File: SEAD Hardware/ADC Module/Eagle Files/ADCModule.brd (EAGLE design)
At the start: 44.9 x 48.9 mm, 49 parts, among them IC2 93-C46AST, U1 LP2989_DGK_8, X1 52885-0374

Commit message: More layout work.
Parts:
- moved C19 18.3 mm to (2.50, 9.70), turned to 0 degrees
- moved U1 18.0 mm to (2.60, 5.70)
- moved C18 16.8 mm to (4.80, 2.90), turned to 270 degrees
- moved C7 16.7 mm to (2.50, 1.80)
- moved L2 13.1 mm to (8.90, 9.50)
- moved C24 13.1 mm to (8.90, 11.1)
- moved C12 13.0 mm to (32.9, 7.20)
- moved C11 13.0 mm to (26.3, 7.12)
- moved C15 13.0 mm to (40.4, 16.1)
- moved C16 13.0 mm to (40.4, 13.3)
- moved C14 13.0 mm to (40.4, 19.8)
- moved R6 13.0 mm to (2.50, 22.7)
- moved R7 13.0 mm to (2.50, 24.2)
- moved C23 13.0 mm to (14.3, 11.1)
- moved LED1 13.0 mm to (39.3, 9.87)
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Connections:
- removed net N$24: C18.2, C7.1, U1.3
- net GND: now also C18.2, C7.1, U1.3
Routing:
- net CANRX: track 0.00 -> 51.4 mm, vias 0 -> 3
- net CANTX: track 0.00 -> 46.3 mm, vias 0 -> 1
- net A0: track 0.00 -> 26.4 mm, vias 0 -> 2
- net WR*: track 0.00 -> 18.3 mm, vias 0 -> 2
- net RD*: track 0.00 -> 17.0 mm, vias 0 -> 2
- net VDD5V0_D: track 0.00 -> 16.9 mm
- net D4: track 5.34 -> 20.7 mm, vias 0 -> 2
- net D3: track 3.70 -> 18.8 mm, vias 0 -> 2
- net CS*: track 0.00 -> 13.2 mm
- net N$11: track 25.1 -> 12.0 mm
- net N$10: track 25.0 -> 11.9 mm
- net USB_UART_RX: track 19.3 -> 31.4 mm
- net USB_UART_TX: track 18.7 -> 30.5 mm
- net D2: track 0.00 -> 11.6 mm, vias 0 -> 2
- net D7: track 11.5 -> 22.9 mm
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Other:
- board size 44.9 x 48.9 mm -> 44.9 x 35.9 mm

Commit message: Finished DAQ revision.
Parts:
- added C25, C26, C27, C28: .1uF, SensorCape:0805
- moved C20 8.81 mm to (15.1, 30.9), turned to 180 degrees
- moved C13 8.61 mm to (38.3, 33.6), turned to 270 degrees
- moved C9 7.20 mm to (36.7, 33.6), turned to 270 degrees
- moved C15 6.48 mm to (41.4, 22.5)
- moved LED1 6.32 mm to (41.3, 15.9)
- moved R3 6.32 mm to (43.0, 15.9)
- moved C16 6.08 mm to (41.4, 19.3)
- moved U$1 6.08 mm to (31.9, 22.5)
- moved C1 6.00 mm to (35.0, 33.6)
- moved C2 6.00 mm to (27.0, 33.6)
- moved U$2 6.00 mm to (31.0, 33.6)
- moved C14 5.59 mm to (41.4, 25.3)
- moved C11 5.10 mm to (27.3, 12.1)
- moved C17 5.10 mm to (30.5, 12.1)
- moved C12 5.10 mm to (33.9, 12.2)
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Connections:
- net VDD1V8_D renamed VCC1V8_D
- net CANRX: no longer X1.7
- net CANTX: no longer X1.9
- net GND: now also C25.1, C26.1, C27.1, C28.1
- net VDD3V3_D: now also C25.2, C26.2, C27.2, C28.2
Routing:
- net VDD5V0_D: track 16.9 -> 97.0 mm, vias 0 -> 2
- net CANRX: track 51.4 -> 0.00 mm, vias 3 -> 0
- net CANTX: track 46.3 -> 0.00 mm, vias 1 -> 0
- net VDD3V3_D: track 19.0 -> 64.3 mm, vias 0 -> 21
- net GND: track 33.4 -> 21.8 mm, vias 12 -> 11
- net WR*: track 18.3 -> 7.55 mm, vias 2 -> 0
- net MCLR: track 3.24 -> 13.6 mm
- net RD*: track 17.0 -> 7.59 mm, vias 2 -> 0
- net D0: track 9.63 -> 17.6 mm, vias 0 -> 2
- net D3: track 18.8 -> 25.3 mm
- net PGC: track 7.54 -> 13.6 mm
- net MISO: track 21.0 -> 16.2 mm
- net PGD: track 10.9 -> 15.6 mm
- net CS*: track 13.2 -> 17.5 mm, vias 0 -> 2
- net USB_UART_TX: track 30.5 -> 26.4 mm
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- added copper zone on layer 15, net GND
- added copper zone on layer 14, net VDD3V3_D
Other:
- board size 44.9 x 35.9 mm -> 44.9 x 36.3 mm
- board text added: "SEAD DAQ Unit v1.3 (c) Pavlo Manovi - 2014 pavlo.me"
- board text removed: "SEAD DAQ Unit v1.2 (c) Pavlo Manovi - 2014 pavlo.me"

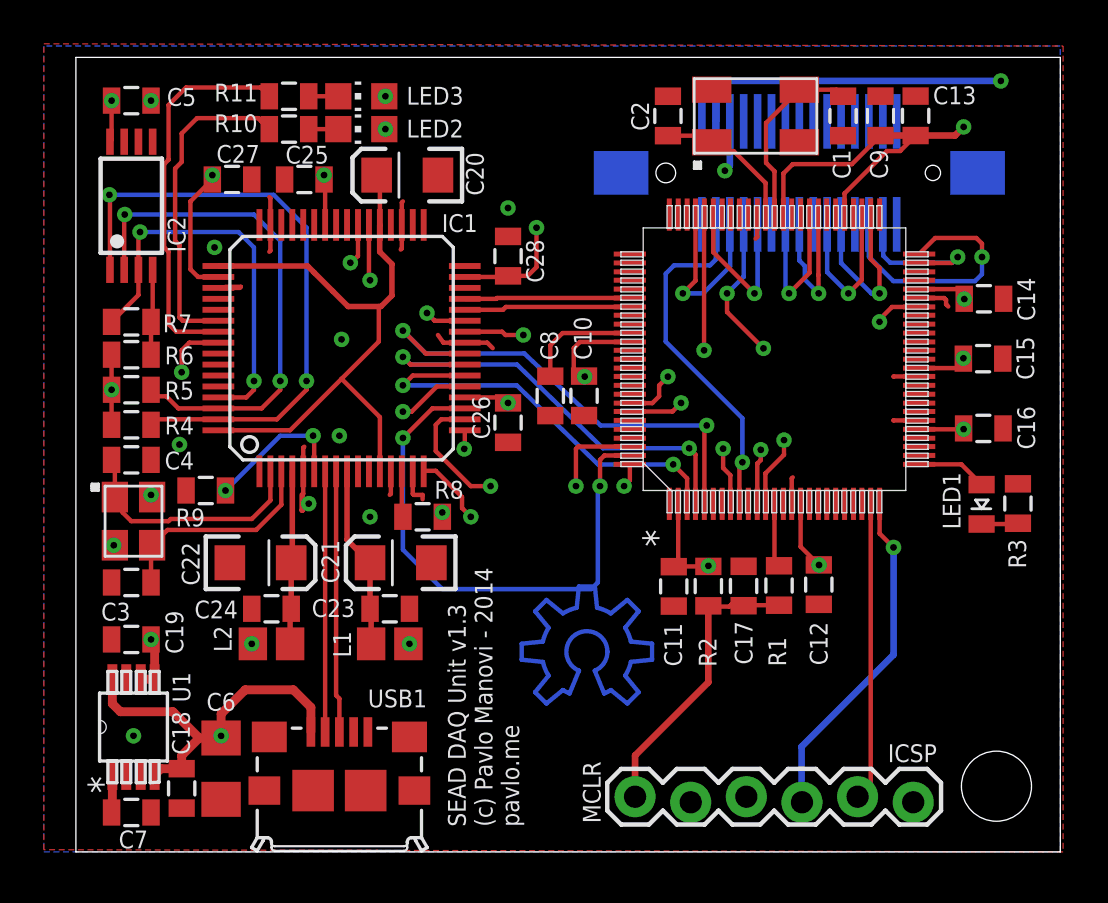
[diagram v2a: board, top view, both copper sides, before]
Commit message: Started ADC Hat. Library additions.
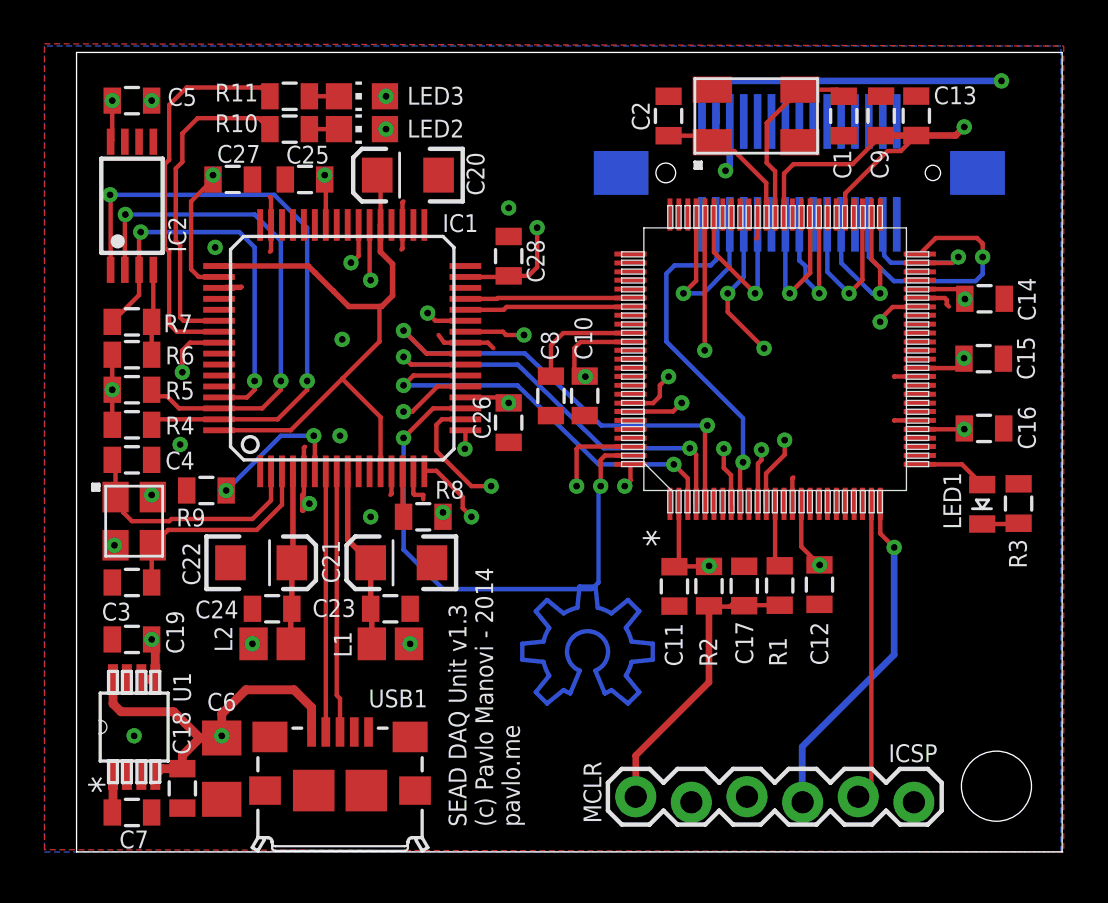
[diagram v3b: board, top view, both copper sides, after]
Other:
- board size 44.9 x 36.3 mm -> 45 x 36.5 mm

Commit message: More board work.
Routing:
- net N$5: track 28.4 -> 0.00 mm
- net N$25: track 0.00 -> 1.55 mm
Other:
- board text removed: "Released under the TAPR OHL v1.0 - http://www.tapr.org/OHL"

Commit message: Started quick PS.
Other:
- outline, holes or cut-outs redrawn
- board text added: "SEAD DAQ Unit v2.0b (c) Pavlo Manovi - 2014 sead.systems / pavlo.me"
- board text removed: "SEAD DAQ Unit v1.3 (c) Pavlo Manovi - 2014 pavlo.me"
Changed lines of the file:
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@@
 <setting verticaltext="up"/>
 </settings>
-<grid distance="0.01" unitdist="mm" unit="mm" style="lines" multiple="1" display="no" altdistance="0.01" altunitdist="mm" altunit="mm"/>
+<grid distance="0.5" unitdist="mm" unit="mm" style="lines" multiple="1" display="no" altdistance="0.01" altunitdist="mm" altunit="mm"/>
 <layers>
 <layer number="1" name="Top" color="4" fill="1" visible="yes" active="yes"/>
@@
 <board>
 <plain>
-<wire x1="45" y1="0" x2="45" y2="36.5" width="0" layer="20"/>
-<wire x1="45" y1="36.5" x2="0" y2="36.5" width="0" layer="20"/>
-<wire x1="0" y1="36.5" x2="0" y2="0" width="0" layer="20"/>
-<wire x1="0" y1="0" x2="45" y2="0" width="0" layer="20"/>
-<text x="20.24" y="1.15" size="0.8128" layer="25" rot="R90">SEAD DAQ Unit v1.3
+<wire x1="0.70710625" y1="0" x2="44.29289375" y2="0" width="0" layer="20"/>
+<wire x1="44.29289375" y1="0" x2="45" y2="0.70710625" width="0" layer="20" curve="90"/>
+<wire x1="45" y1="0.70710625" x2="45" y2="35.79289375" width="0" layer="20"/>
+<wire x1="45" y1="35.79289375" x2="44.29289375" y2="36.5" width="0" layer="20" curve="90"/>
+<wire x1="44.29289375" y1="36.5" x2="0.70710625" y2="36.5" width="0" layer="20"/>
+<wire x1="0.70710625" y1="36.5" x2="0" y2="35.79289375" width="0" layer="20" curve="90"/>
+<wire x1="0" y1="35.79289375" x2="0" y2="0.70710625" width="0" layer="20"/>
+<wire x1="0" y1="0.70710625" x2="0.70710625" y2="0" width="0" layer="20" curve="90"/>
+<text x="42.03" y="9.34" size="0.8128" layer="25" font="vector" rot="R180">SEAD DAQ Unit v2.0b
 (c) Pavlo Manovi - 2014
-pavlo.me</text>
-<text x="37.07" y="4.1" size="0.8128" layer="25">ICSP</text>
+sead.systems / pavlo.me</text>
+<text x="22.77" y="1.24" size="0.8128" layer="25" rot="R90">ICSP</text>
 <text x="23.96" y="1.31" size="0.8128" layer="25" rot="R90">MCLR</text>
 <hole x="42" y="3" drill="3.2"/>
@@
 </element>
 <element name="C11" library="SensorCape" package="0805" value=".1uF" x="27.2968" y="12.1224" smashed="yes" rot="R90">
-<attribute name="NAME" x="27.6713" y="8.4704" size="0.8128" layer="25" ratio="15" rot="R90"/>
+<attribute name="NAME" x="26.3613" y="11.2304" size="0.8128" layer="25" ratio="15" rot="R90"/>
 <attribute name="VALUE" x="28.6938" y="11.1064" size="0.4064" layer="27" rot="R90"/>
 </element>
 <element name="C12" library="SensorCape" package="0805" value=".1uF" x="33.9186" y="12.2036" smashed="yes" rot="R90">
-<attribute name="NAME" x="33.5069" y="10.4984" size="0.8128" layer="25" ratio="15" rot="R270"/>
+<attribute name="NAME" x="35.6331" y="11.2116" size="0.8128" layer="25" ratio="15" rot="R90"/>
 <attribute name="VALUE" x="35.3156" y="11.1876" size="0.4064" layer="27" rot="R90"/>
 </element>
@@
 </element>
 <element name="R1" library="SensorCape" package="0805" value="470" x="32.1028" y="12.1632" smashed="yes" rot="R90">
-<attribute name="NAME" x="32.4273" y="8.4712" size="0.8128" layer="25" ratio="15" rot="R90"/>
+<attribute name="NAME" x="33.0188" y="10.5173" size="0.8128" layer="25" ratio="15" rot="R180"/>
 <attribute name="VALUE" x="33.4998" y="11.1472" size="0.4064" layer="27" rot="R90"/>
 </element>
 <element name="R2" library="SensorCape" package="0805" value="10k" x="28.875" y="12.135" smashed="yes" rot="R90">
-<attribute name="NAME" x="29.2495" y="8.453" size="0.8128" layer="25" ratio="15" rot="R90"/>
+<attribute name="NAME" x="29.077" y="10.5195" size="0.8128" layer="25" ratio="15" rot="R180"/>
 <attribute name="VALUE" x="30.272" y="11.119" size="0.4064" layer="27" rot="R90"/>
 </element>
 <element name="C17" library="SensorCape" package="0805" value=".1uF" x="30.485" y="12.14" smashed="yes" rot="R90">
-<attribute name="NAME" x="30.0805" y="10.532" size="0.8128" layer="25" ratio="15" rot="R270"/>
+<attribute name="NAME" x="29.358" y="9.7005" size="0.8128" layer="25" ratio="15"/>
 <attribute name="VALUE" x="31.882" y="11.124" size="0.4064" layer="27" rot="R90"/>
 </element>
@@
 <wire x1="23.2008" y1="21.7232" x2="23.2068" y2="21.7232" width="0.2032" layer="1"/>
 <wire x1="23.2068" y1="21.7232" x2="23.23" y2="21.7" width="0.2032" layer="1"/>
-<wire x1="33.93" y1="13.1" x2="33.9186" y2="13.1036" width="0" layer="19" extent="1-1"/>
-<wire x1="28.875" y1="13.035" x2="28.88" y2="13.06" width="0" layer="19" extent="1-1"/>
-<wire x1="14.08" y1="34.5" x2="14.13" y2="34.5" width="0" layer="19" extent="1-1"/>
-<wire x1="14.08" y1="33" x2="14.13" y2="33" width="0" layer="19" extent="1-1"/>
-<wire x1="15.18" y1="9.5" x2="15.23" y2="9.5" width="0" layer="19" extent="1-1"/>
-<wire x1="8.08" y1="9.5" x2="8.03" y2="9.5" width="0" layer="19" extent="1-1"/>
+<wire x1="28.875" y1="13.035" x2="28.88" y2="13.035" width="0.4064" layer="1"/>
+<wire x1="28.88" y1="13.035" x2="28.88" y2="13.06" width="0.4064" layer="1"/>
+<wire x1="33.93" y1="13.1" x2="33.9186" y2="13.1" width="0.4064" layer="1"/>
+<wire x1="33.9186" y1="13.1" x2="33.9186" y2="13.1036" width="0.4064" layer="1"/>
+<wire x1="8.08" y1="9.5" x2="8.03" y2="9.5" width="0.4064" layer="1"/>
+<wire x1="15.23" y1="9.5" x2="15.18" y2="9.5" width="0.4064" layer="1"/>
+<wire x1="14.13" y1="33" x2="14.08" y2="33" width="0.4064" layer="1"/>
+<wire x1="14.08" y1="34.5" x2="14.13" y2="34.5" width="0.4064" layer="1"/>
 </signal>
 <signal name="N$14">
@@
 <wire x1="29.19" y1="35" x2="29.23" y2="33.36" width="0.3048" layer="16"/>
 <wire x1="29.23" y1="33.36" x2="29.19" y2="33.35" width="0.3048" layer="16"/>
-<wire x1="6.63" y1="5.3" x2="6.63" y2="5.4" width="0" layer="19" extent="1-14"/>
+<wire x1="6.63" y1="5.4" x2="6.63" y2="5.3" width="0.4064" layer="14"/>
 </signal>
 <signal name="N$23">
